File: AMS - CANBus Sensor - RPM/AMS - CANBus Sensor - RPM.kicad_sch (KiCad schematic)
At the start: 10 parts, among them J5 Power_And_CAN, J6 Conn_02x08_Odd_Even, Q1 IRF9Z34NPBF, U2 178.6165.0001

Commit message: wip for RPM
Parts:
- removed J6: Conn_02x08_Odd_Even, Connector_PinHeader_2.54mm:PinHeader_2x08_P2.54mm_Vertical, symbol Connector_Generic:Conn_02x08_Odd_Even
- removed U2: 178.6165.0001, SamacSys_Parts:17861650001, symbol SamacSys_Parts:178.6165.0001
- added IC4: OPA2340UA_2K5, SamacSys_Parts:SOIC127P600X175-8N, symbol SamacSys_Parts:OPA2340UA_2K5
- added J8: Conn_01x01, Connector_PinHeader_2.54mm:PinHeader_1x01_P2.54mm_Vertical, symbol Connector_Generic:Conn_01x01
- added R10: 120k, Resistor_SMD:R_1206_3216Metric_Pad1.30x1.75mm_HandSolder, symbol Device:R
- added R13: 15k, Resistor_SMD:R_1206_3216Metric_Pad1.30x1.75mm_HandSolder, symbol Device:R
- added R14, R15: 47k, Resistor_SMD:R_1206_3216Metric_Pad1.30x1.75mm_HandSolder, symbol Device:R
- added U2: 3568, SamacSys_Parts:3568, symbol SamacSys_Parts:3568
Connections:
- net +5V: now also IC4.8 (V+)
- net +VDC: now also R10.1, U2.3, U2.4
- net BareMinAtmel328P/PC1-A1: now also IC4.1 (OUT_A), IC4.2 (-INA), R14.1
- net BareMinAtmel328P/PC2-A2: now also IC4.6 (-IN_B), IC4.7 (OUTB), R15.1
- net GND: now also IC4.4 (V-), R13.2, R14.2, R15.2
- net at Q1.3: now also U2.1, U2.2
- new net: IC4.3 (+IN_A), R10.2, R13.1
- new net RPM_Sensor/RPM-Vout: IC4.5 (+INB)
- new net RPM_Sensor/TachIn: J8.1 (Pin_1)
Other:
- added sheet RPM_Sensor (RPM_Sensor.kicad_sch)

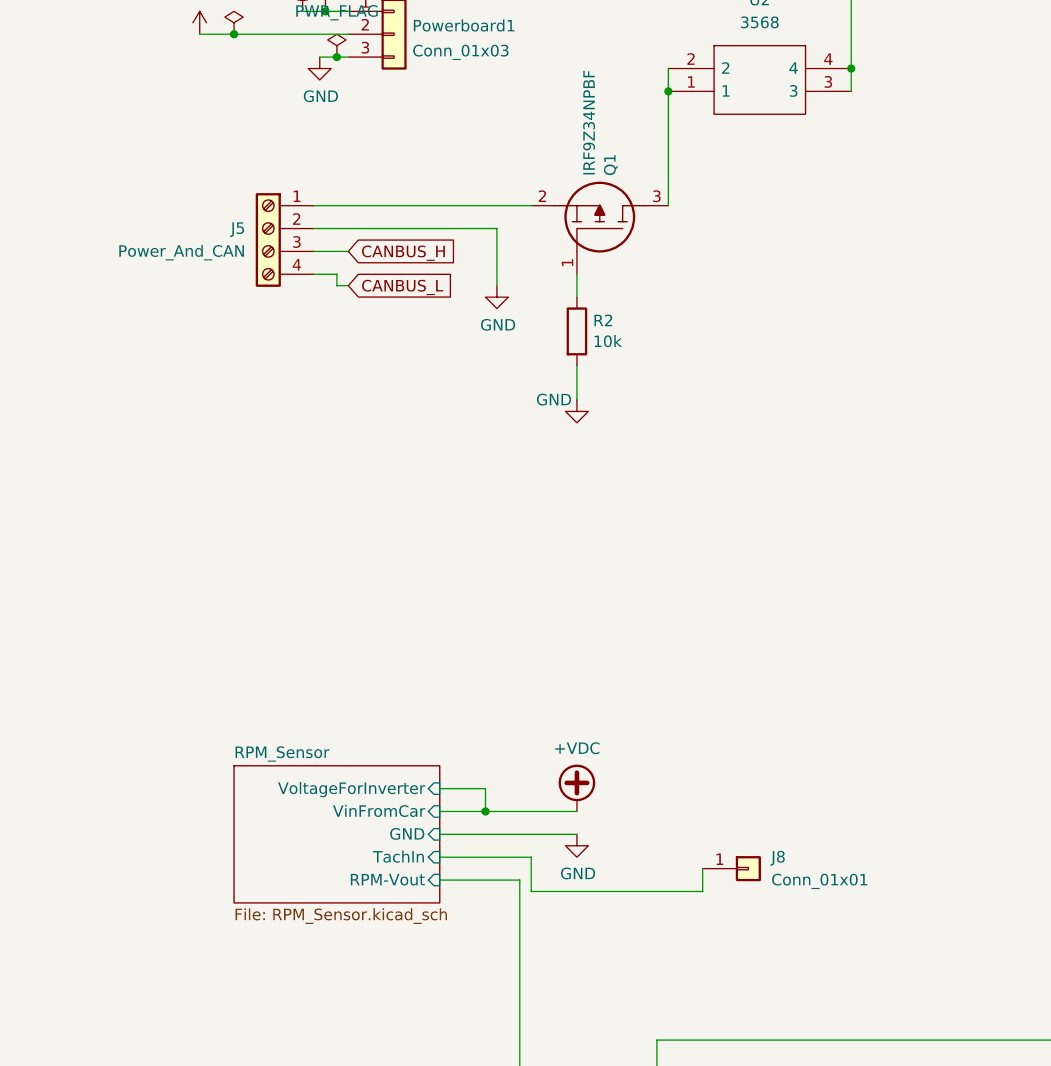
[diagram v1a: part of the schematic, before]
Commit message: RPM Sensor is done.
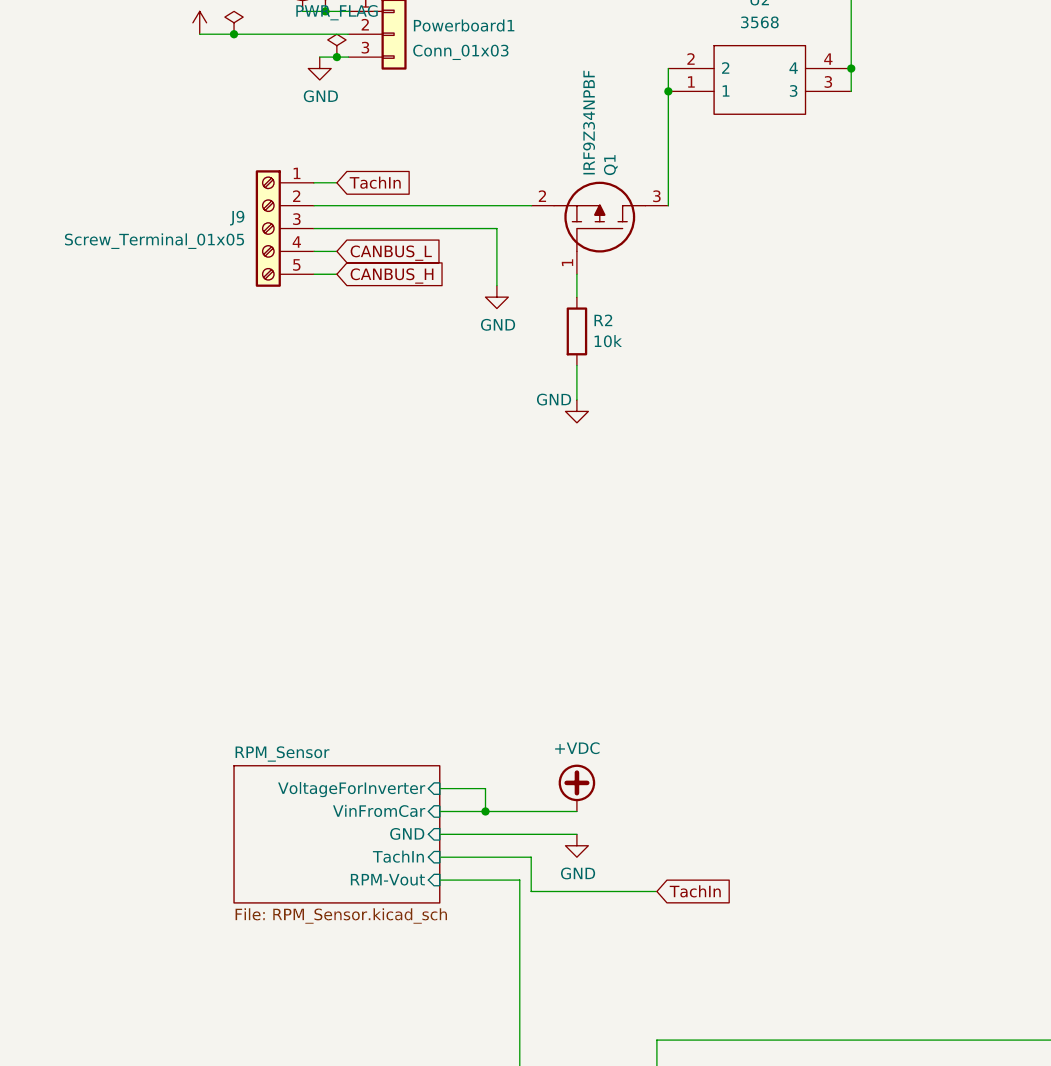
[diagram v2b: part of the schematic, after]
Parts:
- removed J5: Power_And_CAN, TerminalBlock_Phoenix:TerminalBlock_Phoenix_MPT-0,5-4-2.54_1x04_P2.54mm_Horizontal, symbol Connector:Screw_Terminal_01x04
- removed J8: Conn_01x01, Connector_PinHeader_2.54mm:PinHeader_1x01_P2.54mm_Vertical, symbol Connector_Generic:Conn_01x01
- added J9: Screw_Terminal_01x05, TerminalBlock_Phoenix:TerminalBlock_Phoenix_MPT-0,5-5-2.54_1x05_P2.54mm_Horizontal, symbol Connector:Screw_Terminal_01x05
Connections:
- net CANBUS_H: now also J9.5 (Pin_5)
- net CANBUS_L: now also J9.4 (Pin_4)
- net GND: now also J9.3 (Pin_3)
- net at Q1.2: now also J9.2 (Pin_2)
- new net TachIn: J9.1 (Pin_1)
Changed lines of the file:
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@@
-	(wire
-		(pts
-			(xy 38.1 58.42) (xy 38.1 57.15)
-		)
-		(stroke
-			(width 0)
-			(type default)
-		)
-	)
 	(wire
 		(pts
@@
 	(wire
 		(pts
+			(xy 35.56 54.61) (xy 38.1 54.61)
+		)
+		(stroke
+			(width 0)
+			(type default)
+		)
+	)
+	(wire
+		(pts
 			(xy 121.92 38.1) (xy 134.62 38.1)
 		)
@@
 	(wire
 		(pts
+			(xy 35.56 46.99) (xy 38.1 46.99)
+		)
+		(stroke
+			(width 0)
+			(type default)
+		)
+	)
+	(wire
+		(pts
 			(xy 80.01 170.18) (xy 81.28 170.18)
 		)
@@
 	(wire
 		(pts
-			(xy 59.69 125.73) (xy 78.74 125.73)
-		)
-		(stroke
-			(width 0)
-			(type default)
-		)
-	)
-	(wire
-		(pts
 			(xy 166.37 137.16) (xy 166.37 83.82)
 		)
@@
 	(wire
 		(pts
-			(xy 39.37 58.42) (xy 38.1 58.42)
-		)
-		(stroke
-			(width 0)
-			(type default)
-		)
-	)
-	(wire
-		(pts
 			(xy 166.37 83.82) (xy 201.93 83.82)
 		)
@@
 	(wire
 		(pts
-			(xy 35.56 54.61) (xy 39.37 54.61)
-		)
-		(stroke
-			(width 0)
-			(type default)
-		)
-	)
-	(wire
-		(pts
 			(xy 133.35 152.4) (xy 133.35 142.24)
 		)
@@
 	(wire
 		(pts
-			(xy 78.74 125.73) (xy 78.74 123.19)
-		)
-		(stroke
-			(width 0)
-			(type default)
-		)
-	)
-	(wire
-		(pts
 			(xy 64.77 59.69) (xy 64.77 57.15)
 		)
@@
 		(pts
 			(xy 133.35 142.24) (xy 73.66 142.24)
+		)
+		(stroke
+			(width 0)
+			(type default)
+		)
+	)
+	(wire
+		(pts
+			(xy 59.69 125.73) (xy 73.66 125.73)
 		)
 		(stroke
@@
 	(global_label "CANBUS_H"
 		(shape input)
-		(at 39.37 54.61 0)
+		(at 38.1 57.15 0)
 		(fields_autoplaced yes)
 		(effects
@@
 		)
 		(property "Intersheetrefs" "${INTERSHEET_REFS}"
-			(at 52.1524 54.61 0)
+			(at 50.8824 57.15 0)
+			(effects
+				(font
+					(size 1.27 1.27)
+				)
+				(justify left)
+				(hide yes)
+			)
+		)
+	)
+	(global_label "TachIn"
+		(shape input)
+		(at 38.1 46.99 0)
+		(fields_autoplaced yes)
+		(effects
+			(font
+				(size 1.27 1.27)
+			)
+			(justify left)
+		)
+		(property "Intersheetrefs" "${INTERSHEET_REFS}"
+			(at 47.1932 46.99 0)
 			(effects
 				(font
@@
 		)
 	)
+	(global_label "TachIn"
+		(shape input)
+		(at 73.66 125.73 0)
+		(fields_autoplaced yes)
+		(effects
+			(font
+				(size 1.27 1.27)
+			)
+			(justify left)
+		)
+		(property "Intersheetrefs" "${INTERSHEET_REFS}"
+			(at 82.7532 125.73 0)
+			(effects
+				(font
+					(size 1.27 1.27)
+				)
+				(justify left)
+				(hide yes)
+			)
+		)
+	)
 	(global_label "CANBUS_L"
 		(shape input)
@@
 	(global_label "CANBUS_L"
 		(shape input)
-		(at 39.37 58.42 0)
+		(at 38.1 54.61 0)
 		(fields_autoplaced yes)
 		(effects
@@
 		)
 		(property "Intersheetrefs" "${INTERSHEET_REFS}"
-			(at 51.85 58.42 0)
-			(effects
-				(font
-					(size 1.27 1.27)
-				)
-				(justify left)
-				(hide yes)
-			)
-		)
-	)
-	(symbol
-		(lib_id "Connector_Generic:Conn_01x01")
-		(at 83.82 123.19 0)
-		(unit 1)
-		(exclude_from_sim no)
-		(in_bom yes)
-		(on_board yes)
-		(dnp no)
-		(fields_autoplaced yes)
-		(property "Reference" "J8"
-			(at 86.36 121.9199 0)
-			(effects
-				(font
-					(size 1.27 1.27)
-				)
-				(justify left)
-			)
-		)
-		(property "Value" "Conn_01x01"
-			(at 86.36 124.4599 0)
-			(effects
-				(font
-					(size 1.27 1.27)
-				)
-				(justify left)
-			)
-		)
-		(property "Footprint" "Connector_PinHeader_2.54mm:PinHeader_1x01_P2.54mm_Vertical"
-			(at 83.82 123.19 0)
-			(effects
-				(font
-					(size 1.27 1.27)
-				)
-				(hide yes)
-			)
-		)
-		(property "Datasheet" "~"
-			(at 83.82 123.19 0)
-			(effects
-				(font
-					(size 1.27 1.27)
-				)
-				(hide yes)
-			)
-		)
-		(property "Description" "Generic connector, single row, 01x01, script generated (kicad-library-utils/schlib/autogen/connector/)"
-			(at 83.82 123.19 0)
-			(effects
-				(font
-					(size 1.27 1.27)
-				)
-				(hide yes)
-			)
-		)
-		(pin "1"
-		)
-		(instances
-			(project "AMS - CANBus Sensor - RPM"
-				(path "/1c8b441e-37da-469b-a62d-a2093a833f7a"
-					(reference "J8")
-					(unit 1)
-				)
+			(at 50.58 54.61 0)
+			(effects
+				(font
+					(size 1.27 1.27)
+				)
+				(justify left)
+				(hide yes)
 			)
 		)
@@
 	)
 	(symbol
-		(lib_id "Connector:Screw_Terminal_01x04")
-		(at 30.48 52.07 0)
-		(mirror y)
-		(unit 1)
-		(exclude_from_sim no)
-		(in_bom yes)
-		(on_board yes)
-		(dnp no)
-		(property "Reference" "J5"
-			(at 27.94 52.0699 0)
-			(effects
-				(font
-					(size 1.27 1.27)
-				)
-				(justify left)
-			)
-		)
-		(property "Value" "Power_And_CAN"
-			(at 27.94 54.6099 0)
-			(effects
-				(font
-					(size 1.27 1.27)
-				)
-				(justify left)
-			)
-		)
-		(property "Footprint" "TerminalBlock_Phoenix:TerminalBlock_Phoenix_MPT-0,5-4-2.54_1x04_P2.54mm_Horizontal"
-			(at 30.48 52.07 0)
-			(effects
-				(font
-					(size 1.27 1.27)
-				)
-				(hide yes)
-			)
-		)
-		(property "Datasheet" "~"
-			(at 30.48 52.07 0)
-			(effects
-				(font
-					(size 1.27 1.27)
-				)
-				(hide yes)
-			)
-		)
-		(property "Description" "Generic screw terminal, single row, 01x04, script generated (kicad-library-utils/schlib/autogen/connector/)"
-			(at 30.48 52.07 0)
-			(effects
-				(font
-					(size 1.27 1.27)
-				)
-				(hide yes)
-			)
-		)
-		(pin "1"
-		)
-		(pin "2"
-		)
-		(pin "3"
-		)
-		(pin "4"
-		)
-		(instances
-			(project "AMS - CANBus Sensor - RPM"
-				(path "/1c8b441e-37da-469b-a62d-a2093a833f7a"
-					(reference "J5")
-					(unit 1)
-				)
-			)
-		)
-	)
-	(symbol
 		(lib_id "power:GND")
 		(at 128.27 33.02 0)
@@
 					(unit 1)
 				)
+			)
+		)
+	)
+	(symbol
+		(lib_id "Connector:Screw_Terminal_01x05")
+		(at 30.48 52.07 0)
+		(mirror y)
+		(unit 1)
+		(exclude_from_sim no)
+		(in_bom yes)
+		(on_board yes)
+		(dnp no)
+		(property "Reference" "J9"
+			(at 27.94 50.7999 0)
+			(effects
+				(font
+					(size 1.27 1.27)
+				)
+				(justify left)
+			)
+		)
+		(property "Value" "Screw_Terminal_01x05"
+			(at 27.94 53.3399 0)
+			(effects
+				(font
+					(size 1.27 1.27)
+				)
+				(justify left)
+			)
+		)
+		(property "Footprint" "TerminalBlock_Phoenix:TerminalBlock_Phoenix_MPT-0,5-5-2.54_1x05_P2.54mm_Horizontal"
+			(at 30.48 52.07 0)
+			(effects
+				(font
+					(size 1.27 1.27)
+				)
+				(hide yes)
+			)
+		)
+		(property "Datasheet" "~"
+			(at 30.48 52.07 0)
+			(effects
+				(font
+					(size 1.27 1.27)
+				)
+				(hide yes)
+			)
+		)
+		(property "Description" "Generic screw terminal, single row, 01x05, script generated (kicad-library-utils/schlib/autogen/connector/)"
+			(at 30.48 52.07 0)
+			(effects
+				(font
+					(size 1.27 1.27)
+				)
+				(hide yes)
+			)
+		)
+		(pin "2"
+		)
+		(pin "4"
+		)
+		(pin "5"
+		)
+		(pin "3"
+		)
+		(pin "1"
+		)
+		(instances
+			(project "AMS - CANBus Sensor - RPM"
+				(path "/1c8b441e-37da-469b-a62d-a2093a833f7a"
+					(reference "J9")
+					(unit 1)
+				)
